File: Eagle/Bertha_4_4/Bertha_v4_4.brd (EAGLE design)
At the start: 100 x 83.6 mm, 115 parts, among them CON1 JACK_DC_BARREL, CON2 JACK_DC_BARREL, IC1 MCP1703DB, J1 RJ12RIGHTANGLE-I2C, J2 RJ12RIGHTANGLE-I2C, Q1 BSP75, Q2 BSP75, Q3 BSP75, Q4 BSP75, Q5 BSP75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

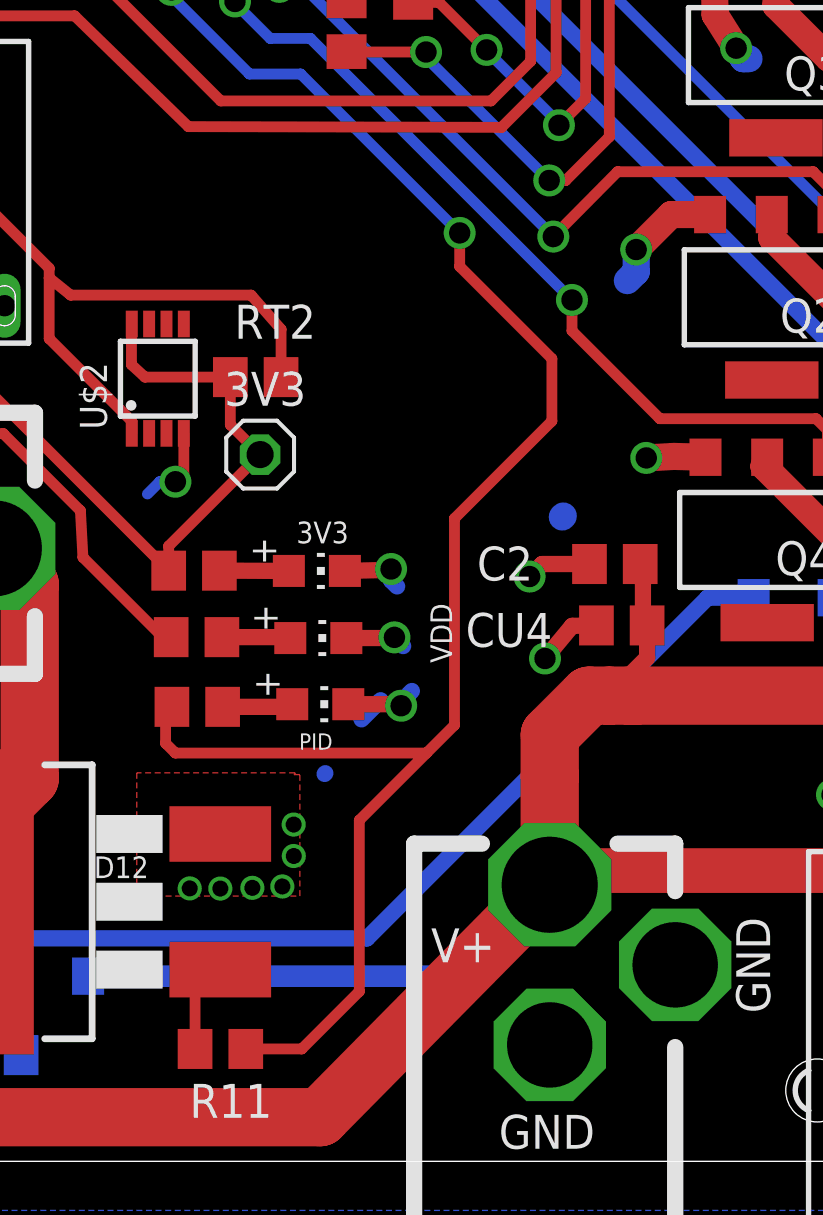
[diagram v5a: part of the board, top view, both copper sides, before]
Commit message: added high side power switch with 5.6V zener on V4.5, drafted hack modif on 4.4, To be tested
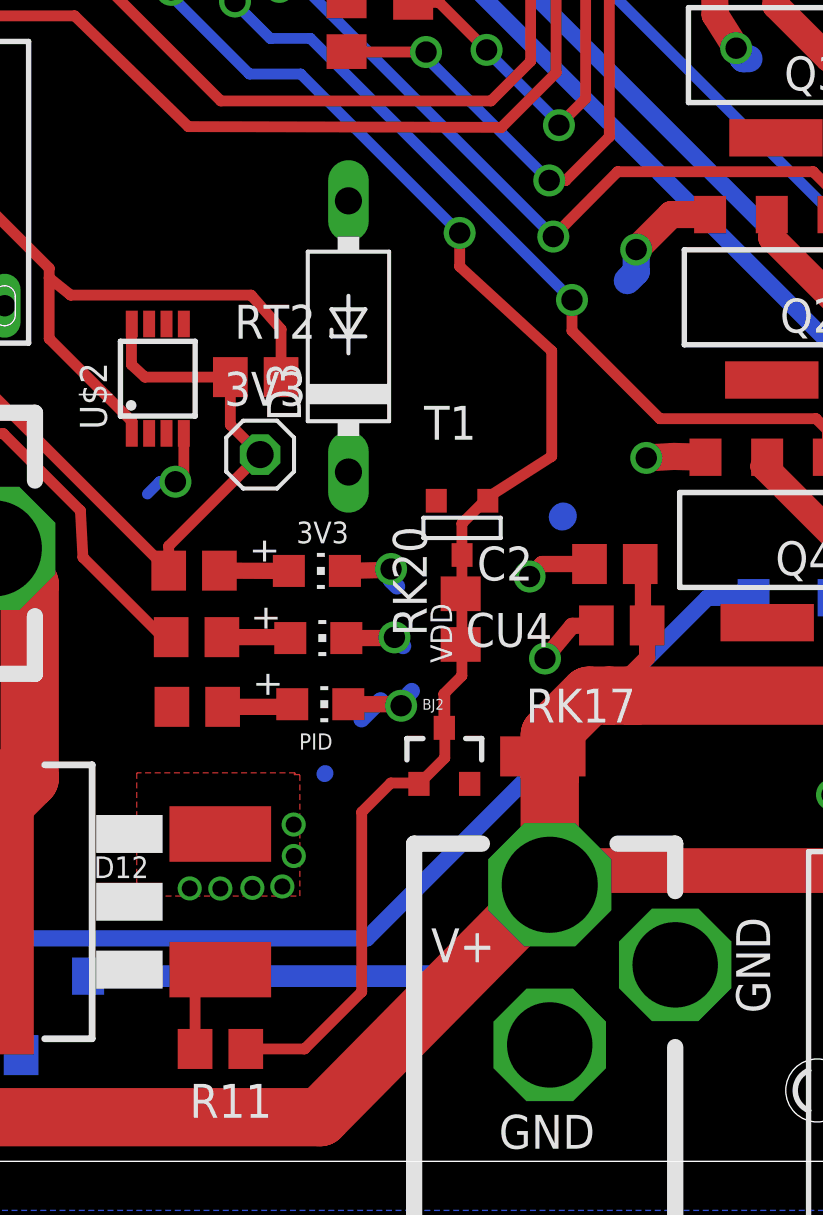
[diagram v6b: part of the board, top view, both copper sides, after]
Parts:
- added BJ2: MMBT4403, SparkFun-DiscreteSemi:SOT23-3
- added D3: (no value), diode:F126Z10
- added RK17, RK20: 1k, rcl:R0805
- added T1: 2n7002, zetex:SOT-23
- R11: value 10k -> 162
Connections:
- new net N$10: BJ2.2, D3.C, RK17.1
- new net N$12: BJ2.1, RK20.1
- new net N$29: RK20.2, T1.1
- new net N$6: BJ2.3, R11.1, RK14.2
- net +12V: now also RK17.2
- net D6*: now also T1.3; no longer R11.1, RK14.2
- net GND: now also D3.A, T1.2
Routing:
- net D6*: track 72.8 -> 45.6 mm
- net N$6: track 0.00 -> 14.8 mm
- net N$12: track 0.00 -> 3.73 mm
